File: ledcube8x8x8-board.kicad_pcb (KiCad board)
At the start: 4 copper layers, 100.8 x 86.8 mm, 187 parts, among them J1 Conn_01x02, J10 molex_53261-0871, J11 104031-0811, J12 molex_53261-0871, J2 molex_53261-0871, J3 molex_53261-0871, J4 molex_53261-0871, J5 molex_53261-0871, J6 molex_53261-0871, J7 molex_53261-0871, J8 molex_53261-0871, J9 molex_53261-0871, Q1 Q_NMOS_GDSD, Q2 Q_NMOS_GDSD, Q3 Q_NMOS_GDSD, Q4 Q_NMOS_GDSD, Q5 Q_NMOS_GDSD, Q6 Q_NMOS_GDSD, Q7 Q_NMOS_GDSD, Q8 Q_NMOS_GDSD, U1 LM1085IS-12, U10 ESP32-DEVKITC-32D, U11 IP4220CZ6, U12 IP4220CZ6, U13 XC9572XL-VQ64, U14 SN74LVCC3245APWR, U15 SN74LVCC3245APWR, U2 STP08CP05MTR, U3 STP08CP05MTR, U4 STP08CP05MTR, U5 STP08CP05MTR, U6 STP08CP05MTR, U7 STP08CP05MTR, U8 STP08CP05MTR, U9 STP08CP05MTR, X1 ASE-40MHz, X2 ASE-25MHz

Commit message: Update footprints
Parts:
- removed C1: 1000uF, Capacitor_SMD:CP_Elec_16x22
- removed C10, C11, C12, C13, C14, C17, C21, C22, C23, C24, C28, C29, C30, C31, C7, C8, C9: 100nF, Capacitor_SMD:C_0805_2012Metric_Pad1.15x1.40mm_HandSolder
- removed C15: 4.7uF, Capacitor_SMD:C_0805_2012Metric_Pad1.15x1.40mm_HandSolder
- removed C16: 10uF, Capacitor_SMD:C_0805_2012Metric_Pad1.15x1.40mm_HandSolder
- removed C18, C19, C20, C25, C26, C27: 10nF, Capacitor_SMD:C_0805_2012Metric_Pad1.15x1.40mm_HandSolder
- removed C2, C5: 10uF, Capacitor_Tantalum_SMD:CP_EIA-3216-12_Kemet-S_Pad1.58x1.35mm_HandSolder
- removed C3: 150uF, Capacitor_SMD:CP_Elec_10x10
- removed C4: 100uF, Capacitor_SMD:CP_Elec_5x5.3
- removed C6: 1uF, Capacitor_SMD:C_0603_1608Metric_Pad1.05x0.95mm_HandSolder
- removed D1, D3: GREEN, Resistor_SMD:R_0805_2012Metric_Pad1.15x1.40mm_HandSolder
- removed D2: RED, Resistor_SMD:R_0805_2012Metric_Pad1.15x1.40mm_HandSolder
- removed D4, D5: ORANGE, Resistor_SMD:R_0805_2012Metric_Pad1.15x1.40mm_HandSolder
- removed H1, H2, H3, H4: MountingHole_Pad, MountingHole:MountingHole_4.3mm_M4_Pad_Via
- removed J1: Conn_01x02, Connector_Molex:Molex_KK-254_AE-6410-02A_1x02_P2.54mm_Vertical
- removed J10, J12, J2, J3, J4, J5, J6, J7, J8, J9: molex_53261-0871, Connector_Molex:Molex_PicoBlade_53261-0871_1x08-1MP_P1.25mm_Horizontal
- removed J11: 104031-0811, MOLEX_104031-0811
- removed NT1, NT2, NT3, NT4, NT5, NT6: Net-Tie_2, NetTie:NetTie-2_SMD_Pad0.5mm
- removed Q1, Q2, Q3, Q4, Q5, Q6, Q7, Q8: Q_NMOS_GDSD, Package_TO_SOT_SMD:SOT-223
- removed R1: 121, Resistor_SMD:R_0603_1608Metric_Pad1.05x0.95mm_HandSolder
- removed R10, R11, R12, R13, R14, R15, R5, R6, R7, R8, R9: 10K, Resistor_SMD:R_0805_2012Metric_Pad1.15x1.40mm_HandSolder
- removed R100, R101, R4, R98, R99: 1K, Resistor_SMD:R_0603_1608Metric_Pad1.05x0.95mm_HandSolder
- removed R102, R103, R104, R80: 0R, Resistor_SMD:R_0603_1608Metric_Pad0.98x0.95mm_HandSolder
- removed R16, R17, R18, R19, R20, R21, R22, R23, R24, R25, R26, R27, R28, R29, R30, R31, R32, R33, R34, R35, R36, R37, R38, R39, R40, R41, R42, R43, R44, R45, R46, R47, R48, R49, R50, R51, R52, R53, R54, R55, R56, R57, R58, R59, R60, R61, R62, R63, R64, R65, R66, R67, R68, R69, R70, R71, R72, R73, R74, R75, R76, R77, R78, R79: 100, Resistor_SMD:R_0603_1608Metric_Pad1.05x0.95mm_HandSolder
- removed R2: 42.2, Resistor_SMD:R_0603_1608Metric_Pad1.05x0.95mm_HandSolder
- removed R3: 56.2, Resistor_SMD:R_0603_1608Metric_Pad1.05x0.95mm_HandSolder
- removed R81, R82: 0R, Resistor_SMD:R_0603_1608Metric_Pad1.05x0.95mm_HandSolder
- removed R83, R84, R86, R88, R89, R90, R91, R94, R95, R96, R97: 10K, Resistor_SMD:R_0603_1608Metric_Pad1.05x0.95mm_HandSolder
- removed R85, R87: 2K7, Resistor_SMD:R_0603_1608Metric_Pad1.05x0.95mm_HandSolder
- removed R92, R93: 0R, Resistor_SMD:R_1206_3216Metric_Pad1.30x1.75mm_HandSolder
- removed U1: LM1085IS-12, LM1085IS-12:TO254P1524X483-4N
- removed U10: ESP32-DEVKITC-32D, MODULE_ESP32-DEVKITC-32D
- removed U11, U12: IP4220CZ6, SOT95P275X110-6N
- removed U13: XC9572XL-VQ64, Package_QFP:TQFP-64_10x10mm_P0.5mm
- removed U14, U15: SN74LVCC3245APWR, SOP65P640X120-24N
- removed U2, U3, U4, U5, U6, U7, U8, U9: STP08CP05MTR, Package_SO:SOIC-16_3.9x9.9mm_P1.27mm
- removed X1: ASE-40MHz, Oscillator:Oscillator_SMD_Abracon_ASE-4Pin_3.2x2.5mm
- removed X2: ASE-25MHz, Oscillator:Oscillator_SMD_Abracon_ASE-4Pin_3.2x2.5mm
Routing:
- net GND: track 651.6 -> 0.00 mm, vias 57 -> 0
- net /pl.sch/VCC_3V3: track 372.0 -> 0.00 mm, vias 8 -> 0
- net GNDD: track 293.4 -> 0.00 mm, vias 10 -> 0
- net /layer_led_mux.sch/CLK: track 228.0 -> 0.00 mm, vias 8 -> 0
- net /pl.sch/~DATA_OE_5V5: track 204.6 -> 0.00 mm, vias 9 -> 0
- net /pl.sch/VCC_5V0: track 197.1 -> 0.00 mm, vias 29 -> 0
- net /pl.sch/DATA_LE_5V5: track 183.6 -> 0.00 mm, vias 8 -> 0
- net SD_3V3: track 111.1 -> 0.00 mm, vias 5 -> 0
- net /DATA_LED5: track 109.0 -> 0.00 mm, vias 2 -> 0
- net /DATA_LED1: track 102.9 -> 0.00 mm, vias 1 -> 0
- net /DATA_LED3: track 97.4 -> 0.00 mm, vias 1 -> 0
- net /LAYER_SEL1: track 79.6 -> 0.00 mm, vias 1 -> 0
- net /pl.sch/I2C_SDA: track 77.8 -> 0.00 mm, vias 4 -> 0
- net /pl.sch/I2C_SCL: track 76.0 -> 0.00 mm, vias 2 -> 0
- net /DATA_LED2: track 69.1 -> 0.00 mm, vias 1 -> 0
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- removed copper zone on B.Cu, net (none)
- removed copper zone on F.Cu, net (none)
- removed copper zone on In2.Cu, net /pl.sch/VCC_5V0
- removed copper zone on In1.Cu, net GND
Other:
- board outline removed

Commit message: Start with newest PCB routing
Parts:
- added C1: 1000uF, Capacitor_SMD:CP_Elec_16x22, F.Cu at (390.0, 58.8)
- added C10: 100nF, Capacitor_SMD:C_0805_2012Metric_Pad1.18x1.45mm_HandSolder, F.Cu at (320.4, 89.9)
- added C11: 100nF, Capacitor_SMD:C_0805_2012Metric_Pad1.18x1.45mm_HandSolder, F.Cu at (354.1, 62.7)
- added C12: 100nF, Capacitor_SMD:C_0805_2012Metric_Pad1.18x1.45mm_HandSolder, F.Cu at (315.6, 90.5)
- added C13: 100nF, Capacitor_SMD:C_0805_2012Metric_Pad1.18x1.45mm_HandSolder, F.Cu at (301.2, 90.5)
- added C14: 100nF, Capacitor_SMD:C_0805_2012Metric_Pad1.18x1.45mm_HandSolder, F.Cu at (310.8, 90.5)
- added C15: 4.7uF, Capacitor_SMD:C_0805_2012Metric_Pad1.18x1.45mm_HandSolder, F.Cu at (358.0, 97.6)
- added C16: 100nF, Capacitor_SMD:C_0805_2012Metric_Pad1.18x1.45mm_HandSolder, F.Cu at (417.4, 63.6)
- added C17: 1uF, Capacitor_SMD:C_0603_1608Metric_Pad1.08x0.95mm_HandSolder, F.Cu at (347.0, 114.6)
- added C18: 10nF, Capacitor_SMD:C_0805_2012Metric_Pad1.18x1.45mm_HandSolder, F.Cu at (367.4, 119.8)
- added C19: 10nF, Capacitor_SMD:C_0805_2012Metric_Pad1.18x1.45mm_HandSolder, F.Cu at (372.3, 119.8)
- added C2: 10uF, Capacitor_Tantalum_SMD:CP_EIA-3216-12_Kemet-S_Pad1.58x1.35mm_HandSolder, F.Cu at (397.9, 69.5)
- added C20: 10nF, Capacitor_SMD:C_0805_2012Metric_Pad1.18x1.45mm_HandSolder, F.Cu at (399.8, 102.1)
- added C21: 100nF, Capacitor_SMD:C_0805_2012Metric_Pad1.18x1.45mm_HandSolder, F.Cu at (404.9, 97.6)
- added C22: 100nF, Capacitor_SMD:C_0805_2012Metric_Pad1.18x1.45mm_HandSolder, F.Cu at (386.8, 116.3)
- added C23: 100nF, Capacitor_SMD:C_0805_2012Metric_Pad1.18x1.45mm_HandSolder, F.Cu at (396.2, 105.1)
- added C24: 100nF, Capacitor_SMD:C_0805_2012Metric_Pad1.18x1.45mm_HandSolder, F.Cu at (391.4, 113.0)
- added C25: 10nF, Capacitor_SMD:C_0805_2012Metric_Pad1.18x1.45mm_HandSolder, F.Cu at (396.2, 108.1)
- added C26: 10nF, Capacitor_SMD:C_0805_2012Metric_Pad1.18x1.45mm_HandSolder, F.Cu at (400.1, 97.6)
- added C27: 10nF, Capacitor_SMD:C_0805_2012Metric_Pad1.18x1.45mm_HandSolder, F.Cu at (404.6, 100.6)
- added C28: 100nF, Capacitor_SMD:C_0805_2012Metric_Pad1.18x1.45mm_HandSolder, F.Cu at (395.0, 102.1)
- added C29: 100nF, Capacitor_SMD:C_0805_2012Metric_Pad1.18x1.45mm_HandSolder, F.Cu at (391.4, 107.0)
- added C3: 150uF, Capacitor_SMD:CP_Elec_10x10, F.Cu at (408.3, 68.1)
- added C30: 100nF, Capacitor_SMD:C_0805_2012Metric_Pad1.18x1.45mm_HandSolder, F.Cu at (391.4, 110.0)
- added C31: 100nF, Capacitor_SMD:C_0805_2012Metric_Pad1.18x1.45mm_HandSolder, F.Cu at (401.0, 105.1)
- added C32: 100nF, Capacitor_SMD:C_0805_2012Metric_Pad1.18x1.45mm_HandSolder, F.Cu at (332.5, 117.7)
- added C33: 22uF, Capacitor_SMD:C_0805_2012Metric_Pad1.18x1.45mm_HandSolder, F.Cu at (307.1, 129.4)
- added C34: 4.7uF, Capacitor_SMD:C_0805_2012Metric_Pad1.18x1.45mm_HandSolder, F.Cu at (337.3, 117.7)
- added C4: 100uF, Capacitor_SMD:CP_Elec_5x5.3, F.Cu at (383.3, 71.3)
- added C5: 10uF, Capacitor_Tantalum_SMD:CP_EIA-3216-12_Kemet-S_Pad1.58x1.35mm_HandSolder, F.Cu at (397.9, 75.6)
- added C6: 1uF, Capacitor_SMD:C_0603_1608Metric_Pad1.08x0.95mm_HandSolder, F.Cu at (407.9, 75.2)
- added C7: 100nF, Capacitor_SMD:C_0805_2012Metric_Pad1.18x1.45mm_HandSolder, F.Cu at (344.5, 70.6)
- added C8: 100nF, Capacitor_SMD:C_0805_2012Metric_Pad1.18x1.45mm_HandSolder, F.Cu at (306.0, 90.5)
- added C9: 100nF, Capacitor_SMD:C_0805_2012Metric_Pad1.18x1.45mm_HandSolder, F.Cu at (325.2, 89.9)
- added D1: GREEN, Resistor_SMD:R_0805_2012Metric_Pad1.20x1.40mm_HandSolder, F.Cu at (403.3, 75.5)
- added D2: RED, Resistor_SMD:R_0805_2012Metric_Pad1.20x1.40mm_HandSolder, F.Cu at (386.8, 119.3)
- added D3: GREEN, Resistor_SMD:R_0805_2012Metric_Pad1.20x1.40mm_HandSolder, F.Cu at (396.1, 111.1)
- added D4: ORANGE, Resistor_SMD:R_0805_2012Metric_Pad1.20x1.40mm_HandSolder, F.Cu at (391.6, 116.0)
- added D5: ORANGE, Resistor_SMD:R_0805_2012Metric_Pad1.20x1.40mm_HandSolder, F.Cu at (401.0, 108.1)
- added D6: BAT54A, Package_TO_SOT_SMD:SOT-23, F.Cu at (333.5, 124.4)
- added H1: MountingHole_Pad, MountingHole:MountingHole_4.3mm_M4_Pad_Via, F.Cu at (436.2, 65.0)
- added H2: MountingHole_Pad, MountingHole:MountingHole_4.3mm_M4_Pad_Via, F.Cu at (446.3, 54.8)
- added H3: MountingHole_Pad, MountingHole:MountingHole_4.3mm_M4_Pad_Via, F.Cu at (446.3, 65.0)
- added H4: MountingHole_Pad, MountingHole:MountingHole_4.3mm_M4_Pad_Via, F.Cu at (436.2, 54.8)
- added J1: Conn_01x02, Connector_Molex:Molex_KK-254_AE-6410-02A_1x02_P2.54mm_Vertical, F.Cu at (390.1, 71.8)
- added J10: molex_53261-0871, Connector_Molex:Molex_PicoBlade_53261-0871_1x08-1MP_P1.25mm_Horizontal, F.Cu at (307.8, 85.4)
- added J11: 104031-0811, 104031_uSDcard:MOLEX_104031-0811, F.Cu at (348.5, 102.9)
- added J12: molex_53261-0871, Connector_Molex:Molex_PicoBlade_53261-0871_1x08-1MP_P1.25mm_Horizontal, F.Cu at (374.0, 100.3)
- added J13: hedear, digikey-footprints:PinHeader_1x2_P2.54mm, F.Cu at (300.8, 125.8)
- added J14: hedear, digikey-footprints:PinHeader_1x2_P2.54mm, F.Cu at (307.4, 125.8)
- added J15: 30306-6002HB, 3M_30306-6002HB, F.Cu at (323.5, 112.8)
- added J16: 61201021621, 61201021621, F.Cu at (330.4, 101.5)
- added J2: molex_53261-0871, Connector_Molex:Molex_PicoBlade_53261-0871_1x08-1MP_P1.25mm_Horizontal, F.Cu at (422.5, 84.7)
- added J3: molex_53261-0871, Connector_Molex:Molex_PicoBlade_53261-0871_1x08-1MP_P1.25mm_Horizontal, F.Cu at (307.8, 61.8)
- added J4: molex_53261-0871, Connector_Molex:Molex_PicoBlade_53261-0871_1x08-1MP_P1.25mm_Horizontal, F.Cu at (325.8, 54.0)
- added J5: molex_53261-0871, Connector_Molex:Molex_PicoBlade_53261-0871_1x08-1MP_P1.25mm_Horizontal, F.Cu at (307.8, 69.7)
- added J6: molex_53261-0871, Connector_Molex:Molex_PicoBlade_53261-0871_1x08-1MP_P1.25mm_Horizontal, F.Cu at (325.8, 61.8)
- added J7: molex_53261-0871, Connector_Molex:Molex_PicoBlade_53261-0871_1x08-1MP_P1.25mm_Horizontal, F.Cu at (307.8, 77.5)
- added J8: molex_53261-0871, Connector_Molex:Molex_PicoBlade_53261-0871_1x08-1MP_P1.25mm_Horizontal, F.Cu at (307.8, 54.0)
- added J9: molex_53261-0871, Connector_Molex:Molex_PicoBlade_53261-0871_1x08-1MP_P1.25mm_Horizontal, F.Cu at (343.8, 54.0)
- added MOD1: ESP32-WROOM-32, digikey-footprints:ESP32-WROOM-32D, F.Cu at (309.1, 112.7)
- added NT1: Net-Tie_2, NetTie:NetTie-2_SMD_Pad0.5mm, F.Cu at (456.0, 52.8)
- added NT2: Net-Tie_2, NetTie:NetTie-2_SMD_Pad0.5mm, F.Cu at (452.9, 52.8)
- added NT3: Net-Tie_2, NetTie:NetTie-2_SMD_Pad0.5mm, F.Cu at (462.1, 50.8)
- added NT4: Net-Tie_2, NetTie:NetTie-2_SMD_Pad0.5mm, F.Cu at (459.0, 50.8)
- added NT5: Net-Tie_2, NetTie:NetTie-2_SMD_Pad0.5mm, F.Cu at (456.0, 50.8)
- added NT6: Net-Tie_2, NetTie:NetTie-2_SMD_Pad0.5mm, F.Cu at (452.9, 50.8)
- added Q1: Q_NMOS_GDSD, Package_TO_SOT_SMD:SOT-223, F.Cu at (418.4, 100.7)
- added Q2: Q_NMOS_GDSD, Package_TO_SOT_SMD:SOT-223, F.Cu at (428.2, 92.8)
- added Q3: Q_NMOS_GDSD, Package_TO_SOT_SMD:SOT-223, F.Cu at (446.3, 84.6)
- added Q4: Q_NMOS_GDSD, Package_TO_SOT_SMD:SOT-223, F.Cu at (428.2, 101.1)
- added Q5: Q_NMOS_GDSD, Package_TO_SOT_SMD:SOT-223, F.Cu at (438.1, 92.8)
- added Q6: Q_NMOS_GDSD, Package_TO_SOT_SMD:SOT-223, F.Cu at (436.4, 84.6)
- added Q7: Q_NMOS_GDSD, Package_TO_SOT_SMD:SOT-223, F.Cu at (438.1, 101.1)
- added Q8: Q_NMOS_GDSD, Package_TO_SOT_SMD:SOT-223, F.Cu at (418.4, 92.4)
- added Q9: Q_PMOS_GSD, Package_TO_SOT_SMD:SOT-23, F.Cu at (405.6, 104.4)
- added R1: 121, Resistor_SMD:R_0603_1608Metric_Pad0.98x0.95mm_HandSolder, F.Cu at (417.2, 66.4)
- added R10: 10K, Resistor_SMD:R_0805_2012Metric_Pad1.20x1.40mm_HandSolder, F.Cu at (453.6, 81.9)
- added R100: 1K, Resistor_SMD:R_0603_1608Metric_Pad0.98x0.95mm_HandSolder, F.Cu at (400.7, 110.8)
- added R101: 1K, Resistor_SMD:R_0603_1608Metric_Pad0.98x0.95mm_HandSolder, F.Cu at (400.5, 116.3)
- added R102: 0R, Resistor_SMD:R_0603_1608Metric_Pad0.98x0.95mm_HandSolder, F.Cu at (337.0, 120.4)
- added R103: 0R, Resistor_SMD:R_0603_1608Metric_Pad0.98x0.95mm_HandSolder, F.Cu at (357.7, 100.4)
- added R104: 0R, Resistor_SMD:R_0603_1608Metric_Pad0.98x0.95mm_HandSolder, F.Cu at (341.9, 115.0)
- added R105: 10K, Resistor_SMD:R_0603_1608Metric_Pad0.98x0.95mm_HandSolder, F.Cu at (412.2, 75.2)
- added R106: 0R, Resistor_SMD:R_0603_1608Metric_Pad0.98x0.95mm_HandSolder, F.Cu at (422.0, 61.4)
- added R107: 10K, Resistor_SMD:R_0603_1608Metric_Pad0.98x0.95mm_HandSolder, F.Cu at (357.7, 102.9)
- added R108: 0R, Resistor_SMD:R_0603_1608Metric_Pad0.98x0.95mm_HandSolder, F.Cu at (337.9, 123.0)
- added R109: 0R, Resistor_SMD:R_0603_1608Metric_Pad0.98x0.95mm_HandSolder, F.Cu at (333.4, 127.9)
- added R11: 10K, Resistor_SMD:R_0805_2012Metric_Pad1.20x1.40mm_HandSolder, F.Cu at (445.4, 90.2)
- added R110: 0R, Resistor_SMD:R_0603_1608Metric_Pad0.98x0.95mm_HandSolder, F.Cu at (351.7, 111.7)
- added R111: 0R, Resistor_SMD:R_0603_1608Metric_Pad0.98x0.95mm_HandSolder, F.Cu at (337.9, 125.5)
- added R112: 47K, Resistor_SMD:R_0603_1608Metric_Pad0.98x0.95mm_HandSolder, F.Cu at (357.7, 105.4)
- added R113: 0R, Resistor_SMD:R_0603_1608Metric_Pad0.98x0.95mm_HandSolder, F.Cu at (341.9, 117.5)
- added R114: 0R, Resistor_SMD:R_0603_1608Metric_Pad0.98x0.95mm_HandSolder, F.Cu at (341.9, 120.0)
- added R115: 0R, Resistor_SMD:R_0603_1608Metric_Pad0.98x0.95mm_HandSolder, F.Cu at (342.2, 127.5)
- added R116: 0R, Resistor_SMD:R_1206_3216Metric_Pad1.30x1.75mm_HandSolder, F.Cu at (315.0, 125.4)
- added R117: 10K, Resistor_SMD:R_0805_2012Metric_Pad1.20x1.40mm_HandSolder, F.Cu at (328.9, 128.2)
- added R118: 10K, Resistor_SMD:R_0805_2012Metric_Pad1.20x1.40mm_HandSolder, F.Cu at (347.2, 111.9)
- added R119: 10K, Resistor_SMD:R_0805_2012Metric_Pad1.20x1.40mm_HandSolder, F.Cu at (324.1, 128.2)
- added R12: 10K, Resistor_SMD:R_0805_2012Metric_Pad1.20x1.40mm_HandSolder, F.Cu at (450.1, 90.2)
- added R120: 10K, Resistor_SMD:R_0805_2012Metric_Pad1.20x1.40mm_HandSolder, F.Cu at (332.5, 120.7)
- added R121: 10K, Resistor_SMD:R_0805_2012Metric_Pad1.20x1.40mm_HandSolder, F.Cu at (324.1, 125.3)
- added R122: 10K, Resistor_SMD:R_0805_2012Metric_Pad1.20x1.40mm_HandSolder, F.Cu at (328.9, 125.3)
- added R123: 10K, Resistor_SMD:R_0603_1608Metric_Pad0.98x0.95mm_HandSolder, F.Cu at (405.0, 110.8)
- added R124: 10K, Resistor_SMD:R_0603_1608Metric_Pad0.98x0.95mm_HandSolder, F.Cu at (395.8, 118.8)
- added R13: 10K, Resistor_SMD:R_0805_2012Metric_Pad1.20x1.40mm_HandSolder, F.Cu at (336.0, 82.0)
- added R14: 10K, Resistor_SMD:R_0805_2012Metric_Pad1.20x1.40mm_HandSolder, F.Cu at (363.6, 54.2)
- added R15: 10K, Resistor_SMD:R_0805_2012Metric_Pad1.20x1.40mm_HandSolder, F.Cu at (363.6, 51.2)
- added R16: 100, Resistor_SMD:R_0603_1608Metric_Pad0.98x0.95mm_HandSolder, F.Cu at (344.3, 73.3)
- added R17: 100, Resistor_SMD:R_0603_1608Metric_Pad0.98x0.95mm_HandSolder, F.Cu at (358.7, 62.5)
- added R18: 100, Resistor_SMD:R_0603_1608Metric_Pad0.98x0.95mm_HandSolder, F.Cu at (353.8, 65.5)
- added R19: 100, Resistor_SMD:R_0603_1608Metric_Pad0.98x0.95mm_HandSolder, F.Cu at (362.1, 72.5)
- added R2: 42.2, Resistor_SMD:R_0603_1608Metric_Pad0.98x0.95mm_HandSolder, F.Cu at (397.1, 72.3)
- added R20: 100, Resistor_SMD:R_0603_1608Metric_Pad0.98x0.95mm_HandSolder, F.Cu at (362.5, 70.0)
- added R21: 100, Resistor_SMD:R_0603_1608Metric_Pad0.98x0.95mm_HandSolder, F.Cu at (349.3, 82.9)
- added R22: 100, Resistor_SMD:R_0603_1608Metric_Pad0.98x0.95mm_HandSolder, F.Cu at (338.5, 91.8)
- added R23: 100, Resistor_SMD:R_0603_1608Metric_Pad0.98x0.95mm_HandSolder, F.Cu at (353.6, 78.0)
- added R24: 100, Resistor_SMD:R_0603_1608Metric_Pad0.98x0.95mm_HandSolder, F.Cu at (366.9, 67.5)
- added R25: 100, Resistor_SMD:R_0603_1608Metric_Pad0.98x0.95mm_HandSolder, F.Cu at (353.6, 80.5)
- added R26: 100, Resistor_SMD:R_0603_1608Metric_Pad0.98x0.95mm_HandSolder, F.Cu at (349.3, 85.4)
- added R27: 100, Resistor_SMD:R_0603_1608Metric_Pad0.98x0.95mm_HandSolder, F.Cu at (368.2, 53.5)
- added R28: 100, Resistor_SMD:R_0603_1608Metric_Pad0.98x0.95mm_HandSolder, F.Cu at (344.3, 78.3)
- added R29: 100, Resistor_SMD:R_0603_1608Metric_Pad0.98x0.95mm_HandSolder, F.Cu at (335.8, 84.7)
- added R3: 56.2, Resistor_SMD:R_0603_1608Metric_Pad0.98x0.95mm_HandSolder, F.Cu at (381.0, 76.0)
- added R30: 100, Resistor_SMD:R_0603_1608Metric_Pad0.98x0.95mm_HandSolder, F.Cu at (349.1, 70.3)
- added R31: 100, Resistor_SMD:R_0603_1608Metric_Pad0.98x0.95mm_HandSolder, F.Cu at (329.8, 89.6)
- added R32: 100, Resistor_SMD:R_0603_1608Metric_Pad0.98x0.95mm_HandSolder, F.Cu at (340.6, 81.8)
- added R33: 100, Resistor_SMD:R_0603_1608Metric_Pad0.98x0.95mm_HandSolder, F.Cu at (349.1, 72.8)
- added R34: 100, Resistor_SMD:R_0603_1608Metric_Pad0.98x0.95mm_HandSolder, F.Cu at (368.2, 56.0)
- added R35: 100, Resistor_SMD:R_0603_1608Metric_Pad0.98x0.95mm_HandSolder, F.Cu at (348.6, 75.3)
- added R36: 100, Resistor_SMD:R_0603_1608Metric_Pad0.98x0.95mm_HandSolder, F.Cu at (340.6, 84.3)
- added R37: 100, Resistor_SMD:R_0603_1608Metric_Pad0.98x0.95mm_HandSolder, F.Cu at (344.9, 80.8)
- added R38: 100, Resistor_SMD:R_0603_1608Metric_Pad0.98x0.95mm_HandSolder, F.Cu at (348.6, 77.8)
- added R39: 100, Resistor_SMD:R_0603_1608Metric_Pad0.98x0.95mm_HandSolder, F.Cu at (353.4, 73.0)
- added R4: 1K, Resistor_SMD:R_0603_1608Metric_Pad0.98x0.95mm_HandSolder, F.Cu at (385.3, 76.0)
- added R40: 100, Resistor_SMD:R_0603_1608Metric_Pad0.98x0.95mm_HandSolder, F.Cu at (372.5, 53.5)
- added R41: 100, Resistor_SMD:R_0603_1608Metric_Pad0.98x0.95mm_HandSolder, F.Cu at (353.4, 70.5)
- added R42: 100, Resistor_SMD:R_0603_1608Metric_Pad0.98x0.95mm_HandSolder, F.Cu at (363.0, 62.5)
- added R43: 100, Resistor_SMD:R_0603_1608Metric_Pad0.98x0.95mm_HandSolder, F.Cu at (372.5, 51.0)
- added R44: 100, Resistor_SMD:R_0603_1608Metric_Pad0.98x0.95mm_HandSolder, F.Cu at (363.4, 56.9)
- added R45: 100, Resistor_SMD:R_0603_1608Metric_Pad0.98x0.95mm_HandSolder, F.Cu at (353.8, 68.0)
- added R46: 100, Resistor_SMD:R_0603_1608Metric_Pad0.98x0.95mm_HandSolder, F.Cu at (363.4, 59.4)
- added R47: 100, Resistor_SMD:R_0603_1608Metric_Pad0.98x0.95mm_HandSolder, F.Cu at (335.8, 87.2)
- added R48: 100, Resistor_SMD:R_0603_1608Metric_Pad0.98x0.95mm_HandSolder, F.Cu at (368.2, 51.0)
- added R49: 100, Resistor_SMD:R_0603_1608Metric_Pad0.98x0.95mm_HandSolder, F.Cu at (358.2, 65.5)
- added R5: 10K, Resistor_SMD:R_0805_2012Metric_Pad1.20x1.40mm_HandSolder, F.Cu at (454.9, 87.8)
- added R50: 100, Resistor_SMD:R_0603_1608Metric_Pad0.98x0.95mm_HandSolder, F.Cu at (372.5, 56.0)
- added R51: 100, Resistor_SMD:R_0603_1608Metric_Pad0.98x0.95mm_HandSolder, F.Cu at (349.3, 87.9)
- added R52: 100, Resistor_SMD:R_0603_1608Metric_Pad0.98x0.95mm_HandSolder, F.Cu at (371.2, 66.9)
- added R53: 100, Resistor_SMD:R_0603_1608Metric_Pad0.98x0.95mm_HandSolder, F.Cu at (358.0, 80.5)
- added R54: 100, Resistor_SMD:R_0603_1608Metric_Pad0.98x0.95mm_HandSolder, F.Cu at (344.9, 83.4)
- added R55: 100, Resistor_SMD:R_0603_1608Metric_Pad0.98x0.95mm_HandSolder, F.Cu at (358.2, 68.0)
- added R56: 100, Resistor_SMD:R_0603_1608Metric_Pad0.98x0.95mm_HandSolder, F.Cu at (362.5, 65.0)
- added R57: 100, Resistor_SMD:R_0603_1608Metric_Pad0.98x0.95mm_HandSolder, F.Cu at (340.2, 86.8)
- added R58: 100, Resistor_SMD:R_0603_1608Metric_Pad0.98x0.95mm_HandSolder, F.Cu at (367.8, 58.5)
- added R59: 100, Resistor_SMD:R_0603_1608Metric_Pad0.98x0.95mm_HandSolder, F.Cu at (367.4, 61.9)
- added R6: 10K, Resistor_SMD:R_0805_2012Metric_Pad1.20x1.40mm_HandSolder, F.Cu at (450.1, 93.1)
- added R60: 100, Resistor_SMD:R_0603_1608Metric_Pad0.98x0.95mm_HandSolder, F.Cu at (340.2, 89.3)
- added R61: 100, Resistor_SMD:R_0603_1608Metric_Pad0.98x0.95mm_HandSolder, F.Cu at (357.8, 70.5)
- added R62: 100, Resistor_SMD:R_0603_1608Metric_Pad0.98x0.95mm_HandSolder, F.Cu at (342.8, 91.8)
- added R63: 100, Resistor_SMD:R_0603_1608Metric_Pad0.98x0.95mm_HandSolder, F.Cu at (371.7, 61.0)
- added R64: 100, Resistor_SMD:R_0603_1608Metric_Pad0.98x0.95mm_HandSolder, F.Cu at (366.9, 65.0)
- added R65: 100, Resistor_SMD:R_0603_1608Metric_Pad0.98x0.95mm_HandSolder, F.Cu at (372.1, 58.5)
- added R66: 100, Resistor_SMD:R_0603_1608Metric_Pad0.98x0.95mm_HandSolder, F.Cu at (357.8, 73.0)
- added R67: 100, Resistor_SMD:R_0603_1608Metric_Pad0.98x0.95mm_HandSolder, F.Cu at (344.9, 85.9)
- added R68: 100, Resistor_SMD:R_0603_1608Metric_Pad0.98x0.95mm_HandSolder, F.Cu at (362.5, 67.5)
- added R69: 100, Resistor_SMD:R_0603_1608Metric_Pad0.98x0.95mm_HandSolder, F.Cu at (349.3, 80.3)
- added R7: 10K, Resistor_SMD:R_0805_2012Metric_Pad1.20x1.40mm_HandSolder, F.Cu at (453.6, 84.9)
- added R70: 100, Resistor_SMD:R_0603_1608Metric_Pad0.98x0.95mm_HandSolder, F.Cu at (334.1, 89.7)
- added R71: 100, Resistor_SMD:R_0603_1608Metric_Pad0.98x0.95mm_HandSolder, F.Cu at (353.0, 75.5)
- added R72: 100, Resistor_SMD:R_0603_1608Metric_Pad0.98x0.95mm_HandSolder, F.Cu at (357.3, 75.5)
- added R73: 100, Resistor_SMD:R_0603_1608Metric_Pad0.98x0.95mm_HandSolder, F.Cu at (361.7, 75.5)
- added R74: 100, Resistor_SMD:R_0603_1608Metric_Pad0.98x0.95mm_HandSolder, F.Cu at (344.3, 75.8)
- added R75: 100, Resistor_SMD:R_0603_1608Metric_Pad0.98x0.95mm_HandSolder, F.Cu at (344.5, 88.4)
- added R76: 100, Resistor_SMD:R_0603_1608Metric_Pad0.98x0.95mm_HandSolder, F.Cu at (371.2, 64.4)
- added R77: 100, Resistor_SMD:R_0603_1608Metric_Pad0.98x0.95mm_HandSolder, F.Cu at (358.0, 78.0)
- added R78: 100, Resistor_SMD:R_0603_1608Metric_Pad0.98x0.95mm_HandSolder, F.Cu at (353.6, 83.0)
- added R79: 100, Resistor_SMD:R_0603_1608Metric_Pad0.98x0.95mm_HandSolder, F.Cu at (366.9, 70.0)
- added R8: 10K, Resistor_SMD:R_0805_2012Metric_Pad1.20x1.40mm_HandSolder, F.Cu at (445.4, 96.1)
- added R80: 0R, Resistor_SMD:R_0603_1608Metric_Pad0.98x0.95mm_HandSolder, F.Cu at (350.6, 119.7)
- added R81: 0R, Resistor_SMD:R_0603_1608Metric_Pad0.98x0.95mm_HandSolder, F.Cu at (355.7, 114.2)
- added R82: 0R, Resistor_SMD:R_0603_1608Metric_Pad0.98x0.95mm_HandSolder, F.Cu at (350.6, 117.1)
- added R83: 10K, Resistor_SMD:R_0603_1608Metric_Pad0.98x0.95mm_HandSolder, F.Cu at (342.2, 125.0)
- added R84: 10K, Resistor_SMD:R_0603_1608Metric_Pad0.98x0.95mm_HandSolder, F.Cu at (356.1, 111.7)
- added R85: 2K7, Resistor_SMD:R_0603_1608Metric_Pad0.98x0.95mm_HandSolder, F.Cu at (342.2, 122.5)
- added R86: 10K, Resistor_SMD:R_0603_1608Metric_Pad0.98x0.95mm_HandSolder, F.Cu at (337.8, 128.0)
- added R87: 2K7, Resistor_SMD:R_0603_1608Metric_Pad0.98x0.95mm_HandSolder, F.Cu at (357.7, 107.9)
- added R88: 10K, Resistor_SMD:R_0603_1608Metric_Pad0.98x0.95mm_HandSolder, F.Cu at (346.3, 119.7)
- added R89: 10K, Resistor_SMD:R_0603_1608Metric_Pad0.98x0.95mm_HandSolder, F.Cu at (351.3, 114.6)
- added R9: 10K, Resistor_SMD:R_0805_2012Metric_Pad1.20x1.40mm_HandSolder, F.Cu at (445.4, 93.1)
- added R90: 10K, Resistor_SMD:R_0603_1608Metric_Pad0.98x0.95mm_HandSolder, F.Cu at (333.4, 130.5)
- added R91: 10K, Resistor_SMD:R_0603_1608Metric_Pad0.98x0.95mm_HandSolder, F.Cu at (346.3, 117.1)
- added R92: 0R, Resistor_SMD:R_1206_3216Metric_Pad1.30x1.75mm_HandSolder, F.Cu at (301.7, 129.5)
- added R93: 0R, Resistor_SMD:R_1206_3216Metric_Pad1.30x1.75mm_HandSolder, F.Cu at (341.8, 112.1)
- added R94: 10K, Resistor_SMD:R_0603_1608Metric_Pad0.98x0.95mm_HandSolder, F.Cu at (400.5, 113.8)
- added R95: 10K, Resistor_SMD:R_0603_1608Metric_Pad0.98x0.95mm_HandSolder, F.Cu at (405.5, 107.9)
- added R96: 10K, Resistor_SMD:R_0603_1608Metric_Pad0.98x0.95mm_HandSolder, F.Cu at (396.2, 116.3)
- added R97: 10K, Resistor_SMD:R_0603_1608Metric_Pad0.98x0.95mm_HandSolder, F.Cu at (396.2, 113.8)
- added R98: 1K, Resistor_SMD:R_0603_1608Metric_Pad0.98x0.95mm_HandSolder, F.Cu at (391.4, 118.7)
- added R99: 1K, Resistor_SMD:R_0603_1608Metric_Pad0.98x0.95mm_HandSolder, F.Cu at (376.8, 119.6)
- added U1: LM1085IS-12, LM1085IS-12:TO254P1524X483-4N, F.Cu at (410.7, 55.9)
- added U10: TL3305AF260QG, SW_TL3305AF260QG, F.Cu at (423.1, 54.9)
- added U11: IP4220CZ6, SOT95P275X110-6N, F.Cu at (319.3, 129.1)
- added U12: IP4220CZ6, SOT95P275X110-6N, F.Cu at (314.4, 129.1)
- added U13: XC9572XL-VQ64, Package_QFP:TQFP-64_10x10mm_P0.5mm, F.Cu at (372.2, 111.1)
- added U14: SN74LVCC3245APWR, SOP65P640X120-24N, F.Cu at (384.5, 110.2)
- added U15: SN74LVCC3245APWR, SOP65P640X120-24N, F.Cu at (388.2, 100.8)
- added U16: TS3A27518EPW, Package_SO:TSSOP-24_4.4x7.8mm_P0.65mm, F.Cu at (334.5, 111.5)
- added U2: STP08CP05MTR, Package_SO:SOIC-16_3.9x9.9mm_P1.27mm, F.Cu at (321.0, 71.2)
- added U3: STP08CP05MTR, Package_SO:SOIC-16_3.9x9.9mm_P1.27mm, F.Cu at (339.0, 63.3)
- added U4: STP08CP05MTR, Package_SO:SOIC-16_3.9x9.9mm_P1.27mm, F.Cu at (329.4, 71.2)
- added U5: STP08CP05MTR, Package_SO:SOIC-16_3.9x9.9mm_P1.27mm, F.Cu at (357.0, 55.5)
- added U6: STP08CP05MTR, Package_SO:SOIC-16_3.9x9.9mm_P1.27mm, F.Cu at (321.0, 82.6)
- added U7: STP08CP05MTR, Package_SO:SOIC-16_3.9x9.9mm_P1.27mm, F.Cu at (329.4, 82.6)
- added U8: STP08CP05MTR, Package_SO:SOIC-16_3.9x9.9mm_P1.27mm, F.Cu at (347.4, 63.3)
- added U9: STP08CP05MTR, Package_SO:SOIC-16_3.9x9.9mm_P1.27mm, F.Cu at (337.9, 74.8)
- added X1: ASE-40MHz, Oscillator:Oscillator_SMD_Abracon_ASE-4Pin_3.2x2.5mm, F.Cu at (381.9, 117.1)
- added X2: ASE-25MHz, Oscillator:Oscillator_SMD_Abracon_ASE-4Pin_3.2x2.5mm, F.Cu at (395.1, 98.3)

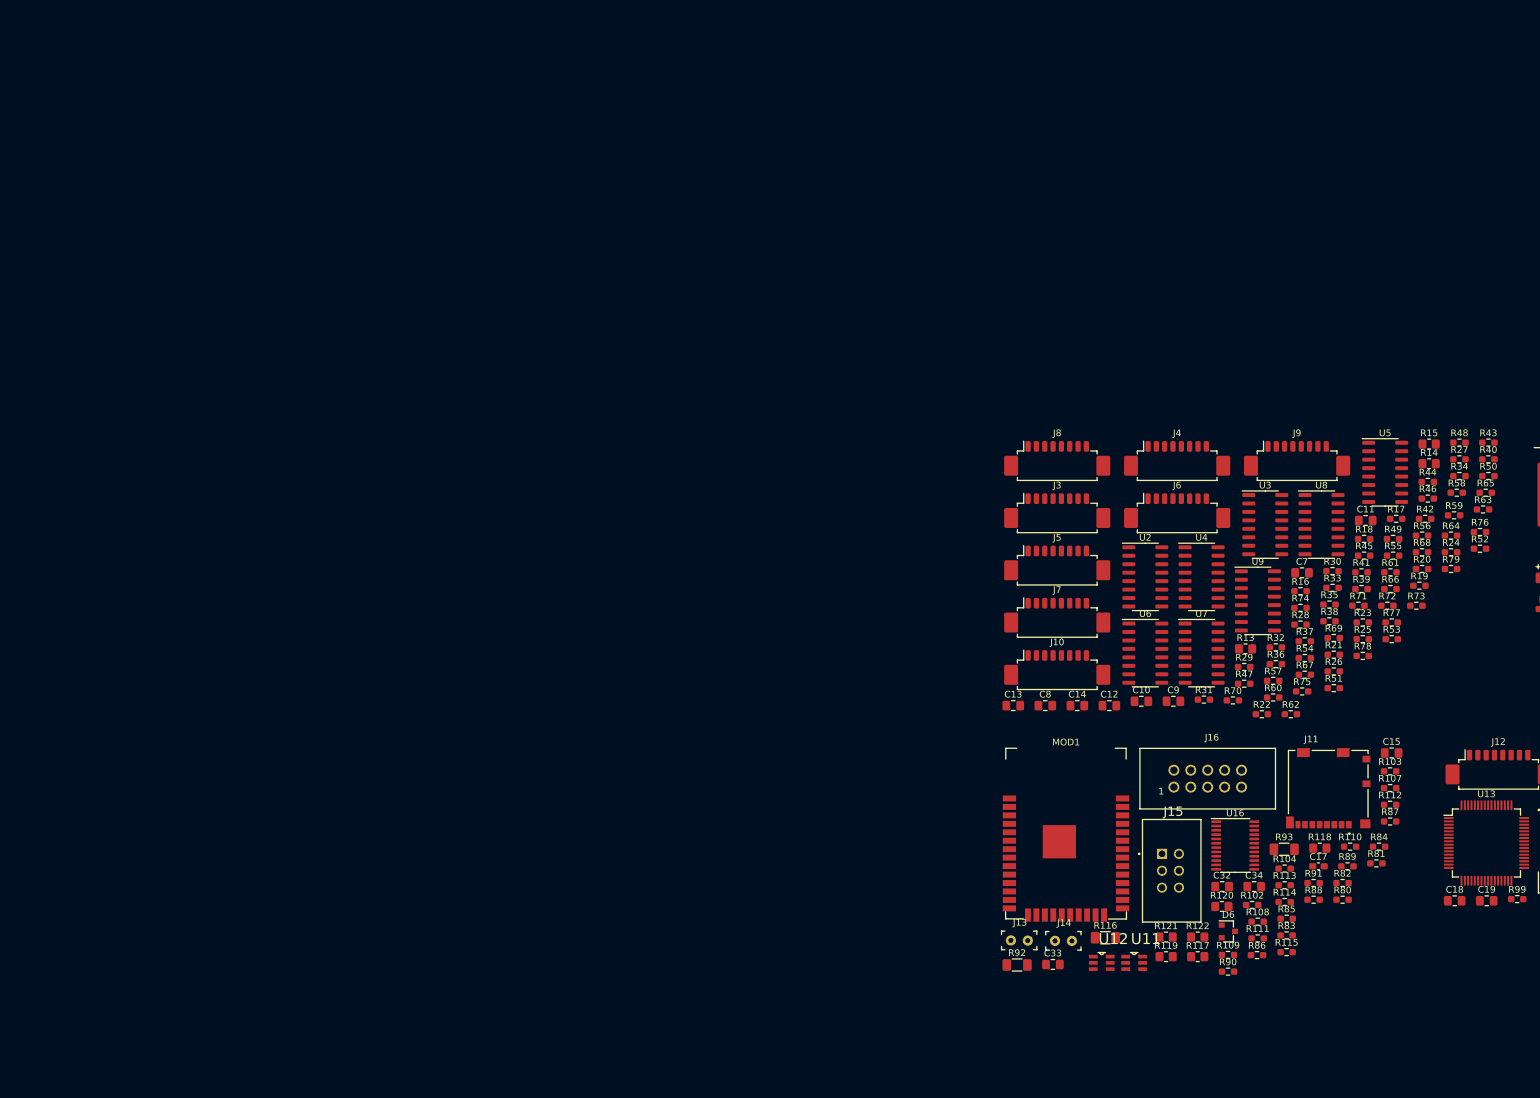
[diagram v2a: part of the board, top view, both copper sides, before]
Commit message: Relative placement of layer multiplexing
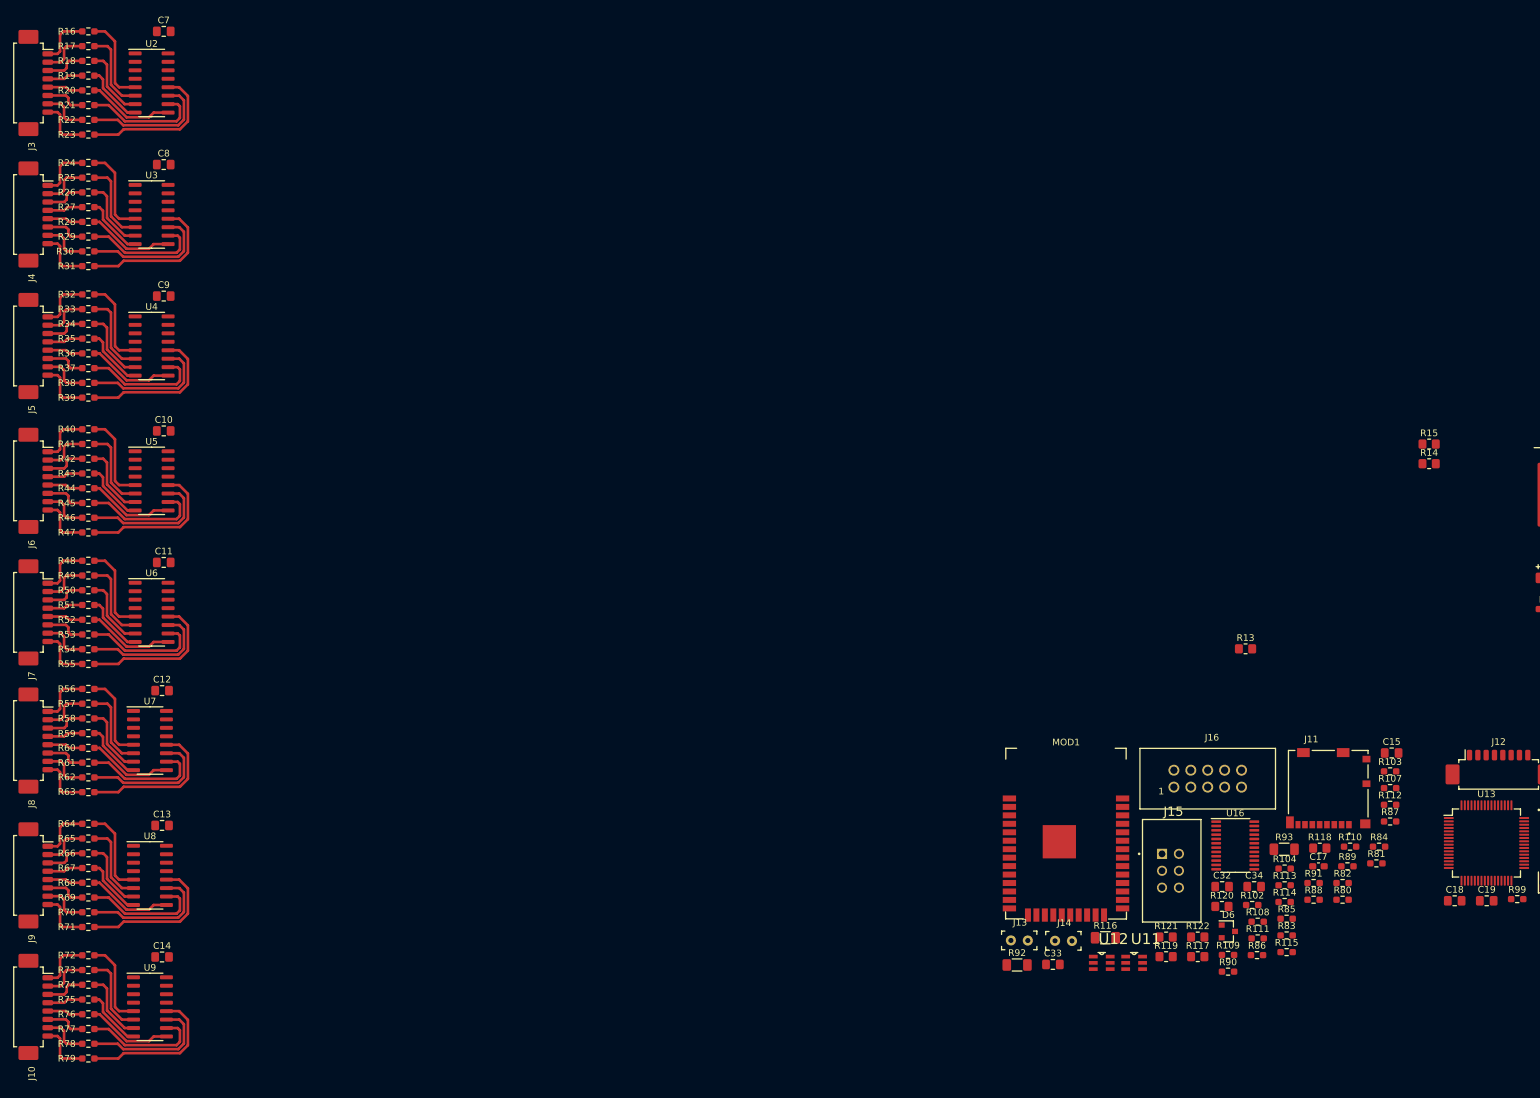
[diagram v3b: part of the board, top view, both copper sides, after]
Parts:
- moved R76 221.2 mm to (162.2, 136.9)
- moved R79 217.4 mm to (162.2, 143.5)
- moved R65 216.2 mm to (162.2, 110.5)
- moved R19 214.1 mm to (162.2, -4.11)
- moved R63 213.7 mm to (162.2, 103.5)
- moved R24 212.8 mm to (162.2, 9.00)
- moved R20 212.8 mm to (162.2, -1.89)
- moved R50 211.0 mm to (162.2, 73.2)
- moved R43 210.3 mm to (162.2, 55.6)
- moved R40 210.3 mm to (162.2, 49.0)
- moved R27 209.4 mm to (162.2, 15.6)
- moved R52 209.3 mm to (162.2, 77.6)
- moved R64 209.2 mm to (162.2, 108.2)
- moved R17 208.8 mm to (162.2, -8.54)
- moved R58 208.3 mm to (162.2, 92.4)
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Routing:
- net Net-(R79-Pad2): track 0.00 -> 22.2 mm
- net Net-(R47-Pad2): track 0.00 -> 22.2 mm
- net Net-(R39-Pad2): track 0.00 -> 22.2 mm
- net Net-(R23-Pad2): track 0.00 -> 22.2 mm
- net Net-(R71-Pad2): track 0.00 -> 22.2 mm
- net Net-(R63-Pad2): track 0.00 -> 22.2 mm
- net Net-(R55-Pad2): track 0.00 -> 22.2 mm
- net Net-(R31-Pad2): track 0.00 -> 22.2 mm
- net Net-(R78-Pad2): track 0.00 -> 19.7 mm
- net Net-(R30-Pad2): track 0.00 -> 19.7 mm
- net Net-(R22-Pad2): track 0.00 -> 19.7 mm
- net Net-(R70-Pad2): track 0.00 -> 19.7 mm
- net Net-(R62-Pad2): track 0.00 -> 19.7 mm
- net Net-(R54-Pad2): track 0.00 -> 19.7 mm
- net Net-(R46-Pad2): track 0.00 -> 19.7 mm
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
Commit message: PCB: Place some macro blocks
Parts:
- added R125: 0R, Resistor_SMD:R_1206_3216Metric_Pad1.30x1.75mm_HandSolder, F.Cu at (76.5, -123.5)
- C1: footprint Capacitor_SMD:CP_Elec_16x22 -> Capacitor_THT:CP_Radial_D12.5mm_P5.00mm
- C11, C12, C13, C14, C15, J10, J7, J8, J9, Q2, Q4, Q6, Q8, R10, R12, R13, R14, R15, R48, R49, R50, R51, R52, R53, R54, R55, R56, R57, R58, R59, R6, R60, R61, R62, R63, R64, R65, R66, R67, R68, R69, R70, R71, R72, R73, R74, R75, R76, R77, R78, R79, R8, R83, R84, R86, R89, R90, R91, U11, U12, U13, U6, U7, U8, U9: moved to B.Cu
- C2, C5: footprint Capacitor_Tantalum_SMD:CP_EIA-3216-12_Kemet-S_Pad1.58x1.35mm_HandSolder -> Capacitor_THT:CP_Radial_D5.0mm_P2.00mm
- C3: footprint Capacitor_SMD:CP_Elec_10x10 -> Capacitor_THT:CP_Radial_D8.0mm_P3.50mm
- C4: footprint Capacitor_SMD:CP_Elec_5x5.3 -> Capacitor_THT:CP_Radial_D6.3mm_P2.50mm
- J1: value Conn_01x02 -> 282836-2; footprint Connector_Molex:Molex_KK-254_AE-6410-02A_1x02_P2.54mm_Vertical -> CONN_282836-2
- J12: value molex_53261-0871 -> 30306-6002HB; footprint Connector_Molex:Molex_PicoBlade_53261-0871_1x08-1MP_P1.25mm_Horizontal -> 3M_30306-6002HB
- moved H3 520.4 mm to (-73.8, 84.2)
- moved R6 511.0 mm to (-32.8, -74.0), turned to 90 degrees
- moved R5 510.0 mm to (-28.5, -74.8), turned to 90 degrees
- moved R7 505.7 mm to (-23.8, -82.2), turned to 90 degrees
- moved R8 498.3 mm to (-23.0, -74.0), turned to 90 degrees
- moved R9 493.2 mm to (-16.8, -79.0), turned to 90 degrees
- moved R10 492.2 mm to (-13.2, -74.0), turned to 90 degrees
- moved R12 482.4 mm to (-3.50, -74.0), turned to 90 degrees
- moved R11 476.7 mm to (-0.50, -78.5), turned to 90 degrees
- moved R1 466.5 mm to (-36.0, -44.2)
- moved NT1 460.7 mm to (1.71, -24.2)
- moved NT2 460.7 mm to (-1.34, -24.2)
- moved NT3 460.7 mm to (7.81, -26.2)
- moved NT4 460.7 mm to (4.76, -26.2)
- moved NT5 460.7 mm to (1.71, -26.2)
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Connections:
- net /pl.sch/DATA_LE_5V5 renamed /pl.sch/DATA_LE_5V0
- net /pl.sch/~DATA_OE_5V5 renamed /pl.sch/~DATA_OE_5V0
- J11 pad 4: GNDD -> SD_3V3
- J12 pad 1: /pl.sch/VCC_3V3 -> Net-(J12-Pad1)
- J12 pad 2: /pl.sch/TCK -> /pl.sch/TDI
- J12 pad 3: /pl.sch/TDO -> /pl.sch/TCK
- J12 pad 5: Net-(J12-Pad5) -> /pl.sch/TDO
- J12 pad 6: /pl.sch/TDI -> GNDD
- U12 pad 3: /ps.sch/SD_CLK -> Net-(J11-Pad3)
- U12 pad 4: /ps.sch/SD_CMD -> Net-(J11-Pad5)
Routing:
- net /pl.sch/DATA_LE_5V0: track 0.00 -> 113.7 mm, vias 0 -> 7
- net /layer_led_mux.sch/CLK: track 0.00 -> 111.9 mm, vias 0 -> 7
- net /pl.sch/~DATA_OE_5V0: track 0.00 -> 107.1 mm, vias 0 -> 4
- net /pl.sch/VCC_3V3: track 0.00 -> 67.6 mm
- net GNDD: track 0.00 -> 57.4 mm
- net GND: track 0.00 -> 56.6 mm
- net /pl.sch/VCC_5V0: track 0.00 -> 33.3 mm
- net SD_3V3: track 0.00 -> 26.1 mm, vias 0 -> 1
- net /layer_selector.sch/LAYER_SEL7: track 0.00 -> 25.8 mm
- net /layer_selector.sch/LAYER_SEL8: track 0.00 -> 24.0 mm, vias 0 -> 1
- net Net-(J11-Pad1): track 0.00 -> 20.1 mm, vias 0 -> 2
- net /layer_selector.sch/LAYER_SEL2: track 0.00 -> 19.7 mm, vias 0 -> 1
- net /layer_selector.sch/LAYER_SEL5: track 0.00 -> 19.1 mm
- net /layer_selector.sch/LAYER_SEL1: track 0.00 -> 18.0 mm
- net /layer_selector.sch/LAYER_SEL6: track 0.00 -> 17.5 mm, vias 0 -> 1
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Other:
- board outline added: 120 x 90 mm
